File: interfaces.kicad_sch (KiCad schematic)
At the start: 125 parts, among them J3 USB-Micro-B-10118192-0001LF, J6 0878311420, J7 61300611121, U1 MTFC16GAPALNA-AIT, U14 XC7A100T-FGG484, U17 USB3300-EZK-TR, U18 USB3300-EZK-TR, U19 FT4232H_QFN, U21 LSF0108RKSR, U22 LSF0101DRYR, U23 ASEMB-24.000MHZ-LC-T, U24 ASEMB-24.000MHZ-LC-T, U6 NVT2008BQ,115, Y1 Oscillator_SMD_12MHz_KX-7

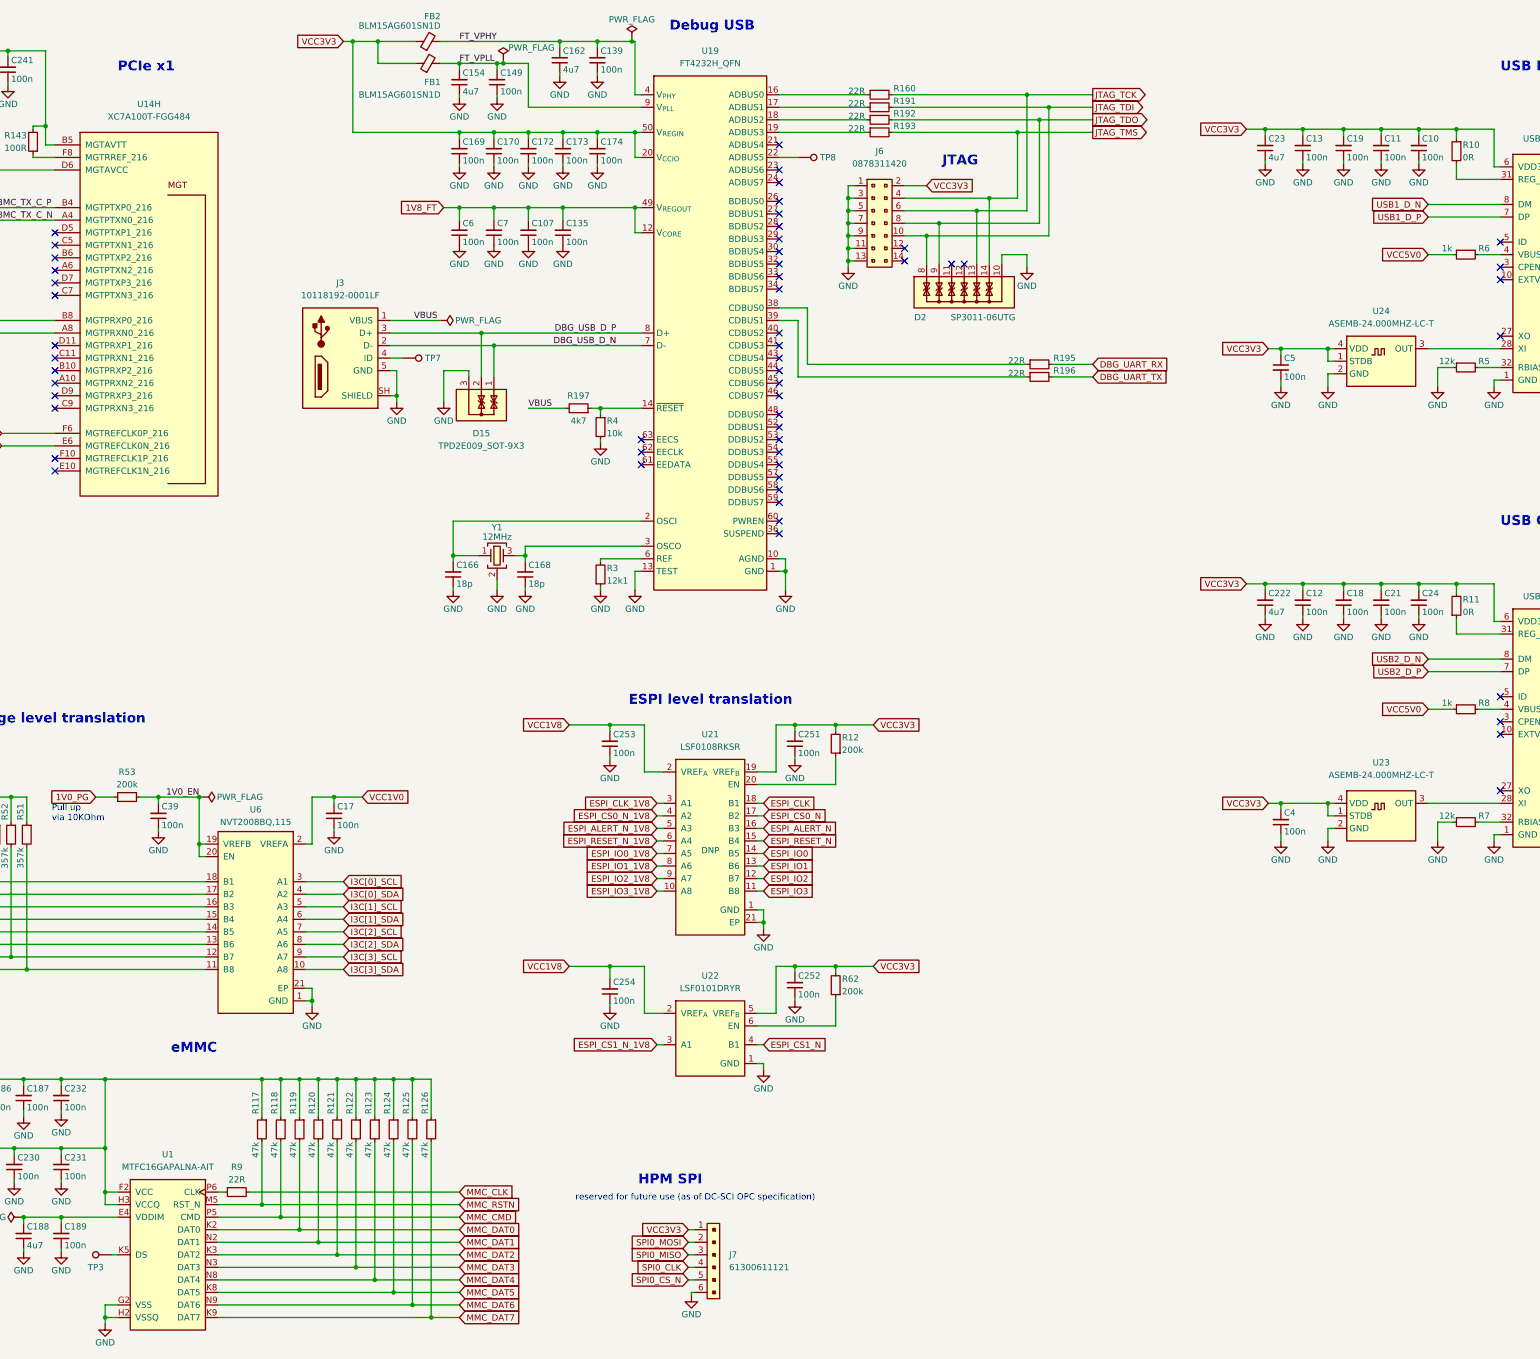
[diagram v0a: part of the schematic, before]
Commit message: [#55652] Fix hotareas
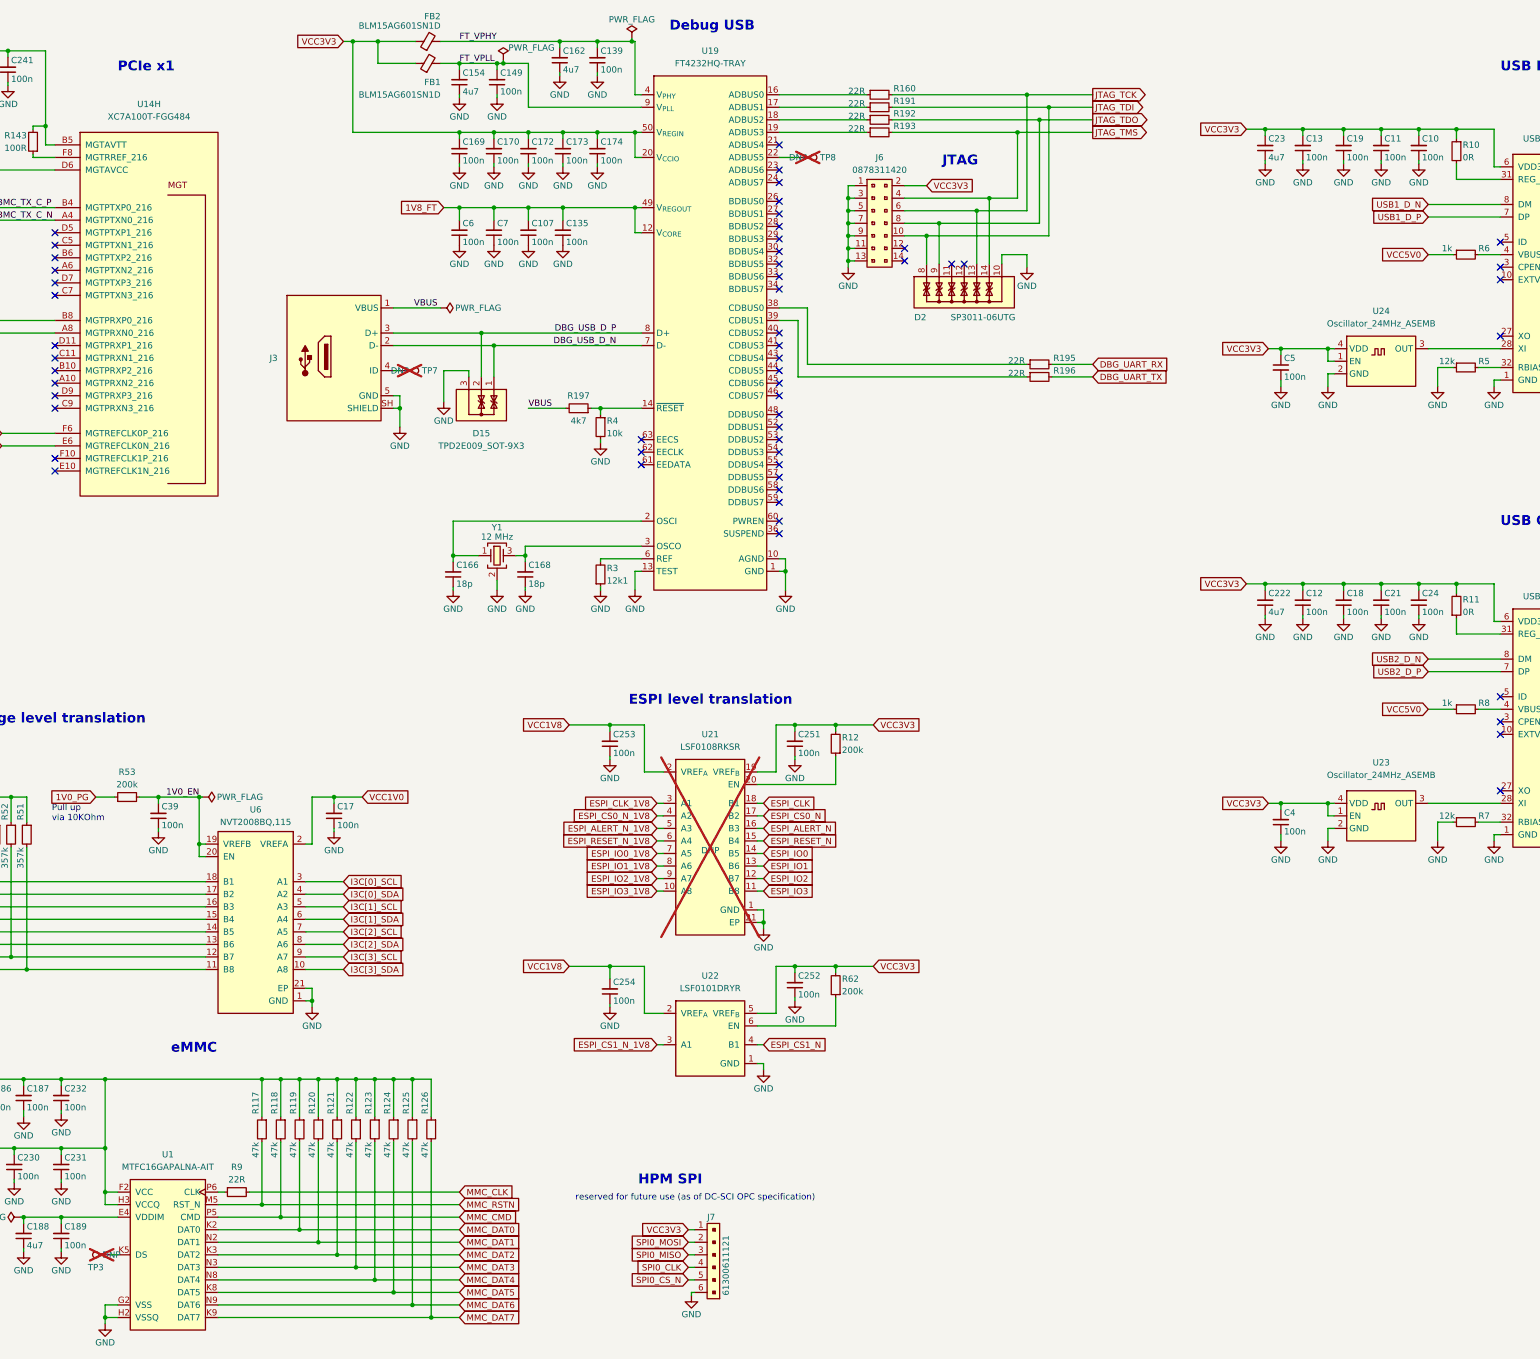
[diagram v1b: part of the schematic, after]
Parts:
- C166, C168: MPN MC0402N180J500CT -> CL05C180JB51PNC; Manufacturer Multicomp -> Samsung Electro-Mechanics
- D2: Manufacturer Littlefuse -> Littelfuse
- FB1, FB2: value FB_600Z_0.3A_0402 -> FB_600Z_0.3A_Murata-BLM15AG_0402; symbol antmicroFerriteBeadsandChips:FB_600Z_0.3A_0402 -> antmicroFerriteBeadsandChips:FB_600Z_0.3A_Murata-BLM15AG_0402
- J3: value USB-Micro-B-10118192-0001LF -> USB-Micro-B_Amphenol_10118192-0001LF; footprint antmicro-footprints:USB_Micro_B_Female_10118192 -> antmicro-footprints:USB-Micro-B_Receptacle_Amphenol_10118192; symbol antmicroUSBDVIHDMIConnectors:USB-Micro-B-10118192-0001LF -> antmicroUSBConnectors:USB-Micro-B_Amphenol_10118192-0001LF; VSD_class (none) -> USB Micro
- J6: value 0878311420 -> PinHeader_2x7_P2mm_Drill1mm_Shrouded; symbol antmicroRectangularConnectorsHeadersMalePins:PinHeader_2x7_P2mm_Drill1mm_Shrouded -> antmicroGenericPinHeaders:PinHeader_2x7_P2mm_Drill1mm_Shrouded
- J7: value 61300611121 -> PinHeader_1x6_P2.54mm_Drill1.1mm; footprint antmicro-footprints:PinHeader_1x6_P2.54mm -> antmicro-footprints:PinHeader_1x6_P2.54mm_Drill1.1mm; symbol antmicroRectangularConnectorsHeadersMalePins:61300611121 -> antmicroGenericPinHeaders:PinHeader_1x6_P2.54mm_Drill1.1mm
- R12, R53, R62: value R_200k_0402-artix-dc-scm -> R_200k_0402
- R45, R46, R47, R48, R49, R50, R51, R52: value R_357k_0402-artix-dc-scm -> R_357k_0402
- TP3, TP7, TP8: value TP_SMD1MM -> TP_1mm_SMD; footprint antmicro-footprints:Testpoint_smd_1mm -> antmicro-footprints:TP_SMD_1mm; now not fitted; now left out of the parts list
- U1: footprint antmicro-footprints:BGA-100_18x14mm_Layout17x10_P1mm -> antmicro-footprints:BGA-170-100_18x14mm_Layout17x10_P1mm; Manufacturer Micron -> Micron Technology
- U14: footprint antmicro-footprints:BGA-484_23x23mm_Layout22x22_P1mm_Xilinx_FGG484 -> antmicro-footprints:BGA-484_23x23mm_Layout22x22_P1mm_FGG484; symbol antmicroMicrocontrollers:XC7A100T-FGG484 -> antmicroFPGAChips:XC7A100T-FGG484; Manufacturer Xilinx -> AMD-Xilinx
- U17, U18: Manufacturer Microchip -> Microchip Technology
- U19: footprint antmicro-footprints:QFN-64_1EP_9x9mm_P0.5mm -> antmicro-footprints:QFN-64-1EP_9x9mm_P0.5mm; Manufacturer FTDI -> FTDI Chip
- U21: now not fitted; now left out of the parts list
- U23, U24: value ASEMB-24.000MHZ-LC-T -> Oscillator_24MHz_ASEMB; footprint antmicro-footprints:Oscillator_SMD_Abracon_ASEM_3.2x2.5mm -> antmicro-footprints:Oscillator_SMD_Abracon_ASEMB_3.2x2.5mm; symbol antmicroOscillators:Oscillator_SMD_24MHz_ASEMB -> antmicroOscillators:Oscillator_24MHz_ASEMB; Val 24MHz -> 24 MHz
- Y1: value Oscillator_SMD_12MHz_KX-7 -> Resonator_12MHz_ABM8G; footprint antmicro-footprints:Oscillator_SMD_Geyer_KX-7-4Pin_3.2x2.5mm -> antmicro-footprints:Resonator_SMD_Abracon_ABM8G_3.2x2.5mm; symbol antmicroCrystals:Oscillator_SMD_12MHz_KX-7 -> antmicroResonators:Resonator_12MHz_ABM8G; MPN ABM8G-12.000MHZ-18-D2Y-T -> ABM8G-12.000MHZ-18-D2Y-T; Val 12MHz -> 12 MHz

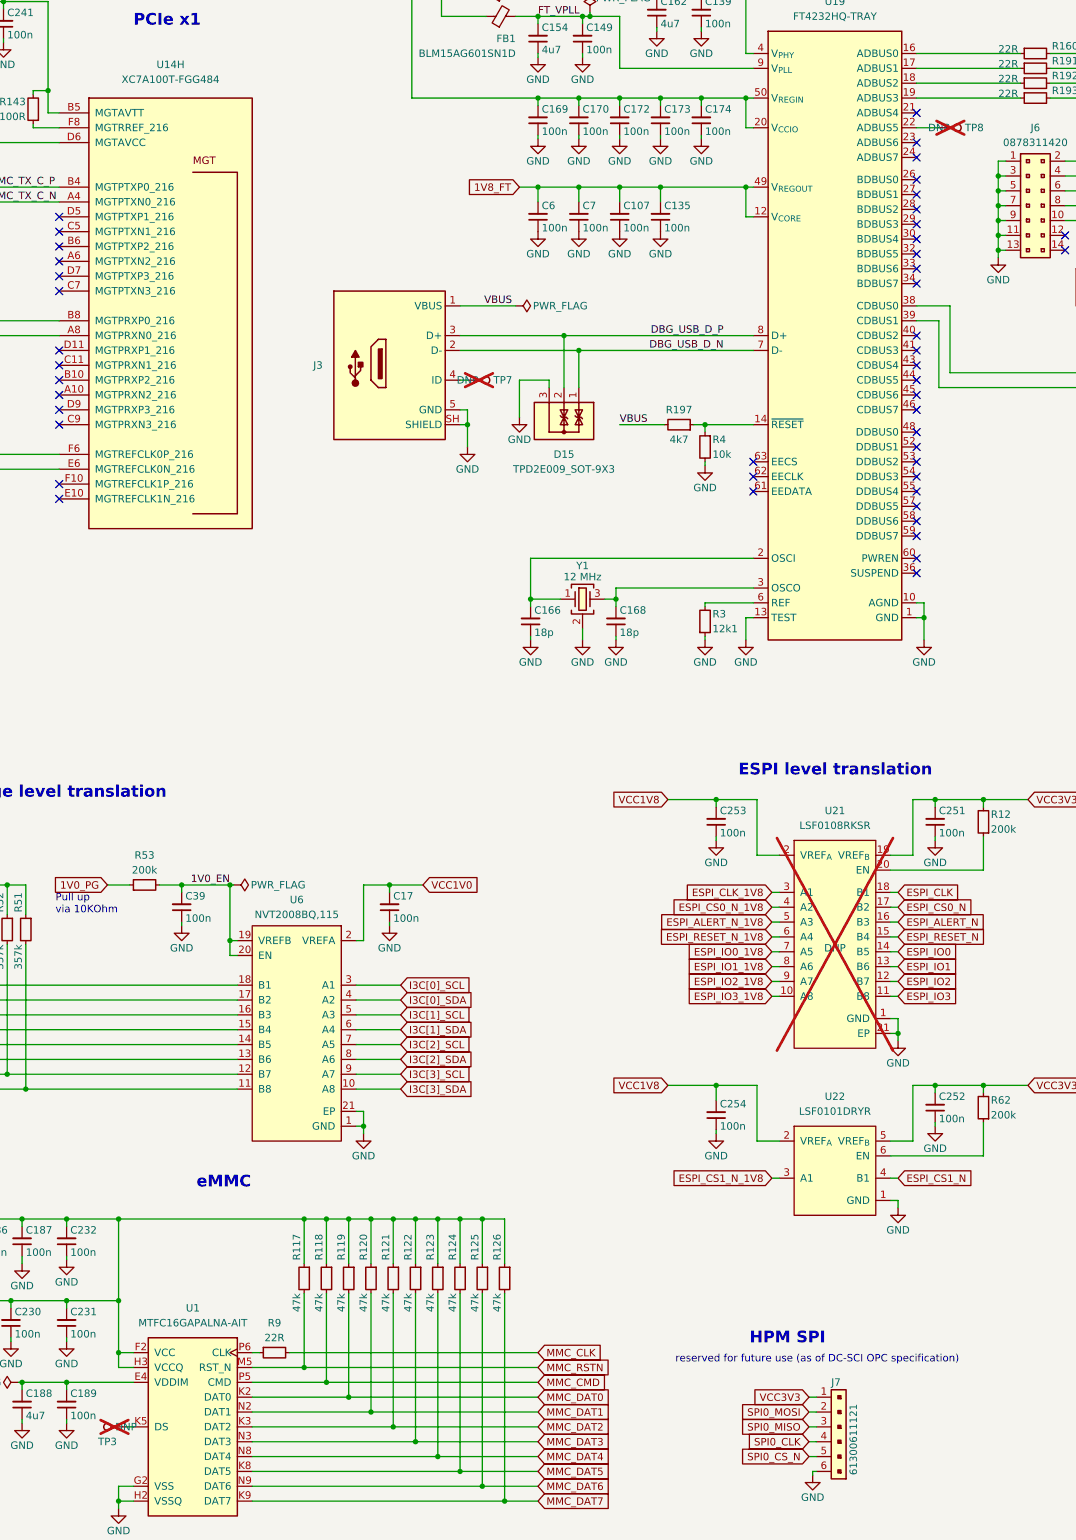
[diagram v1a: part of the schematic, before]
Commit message: [#68236] Update components description
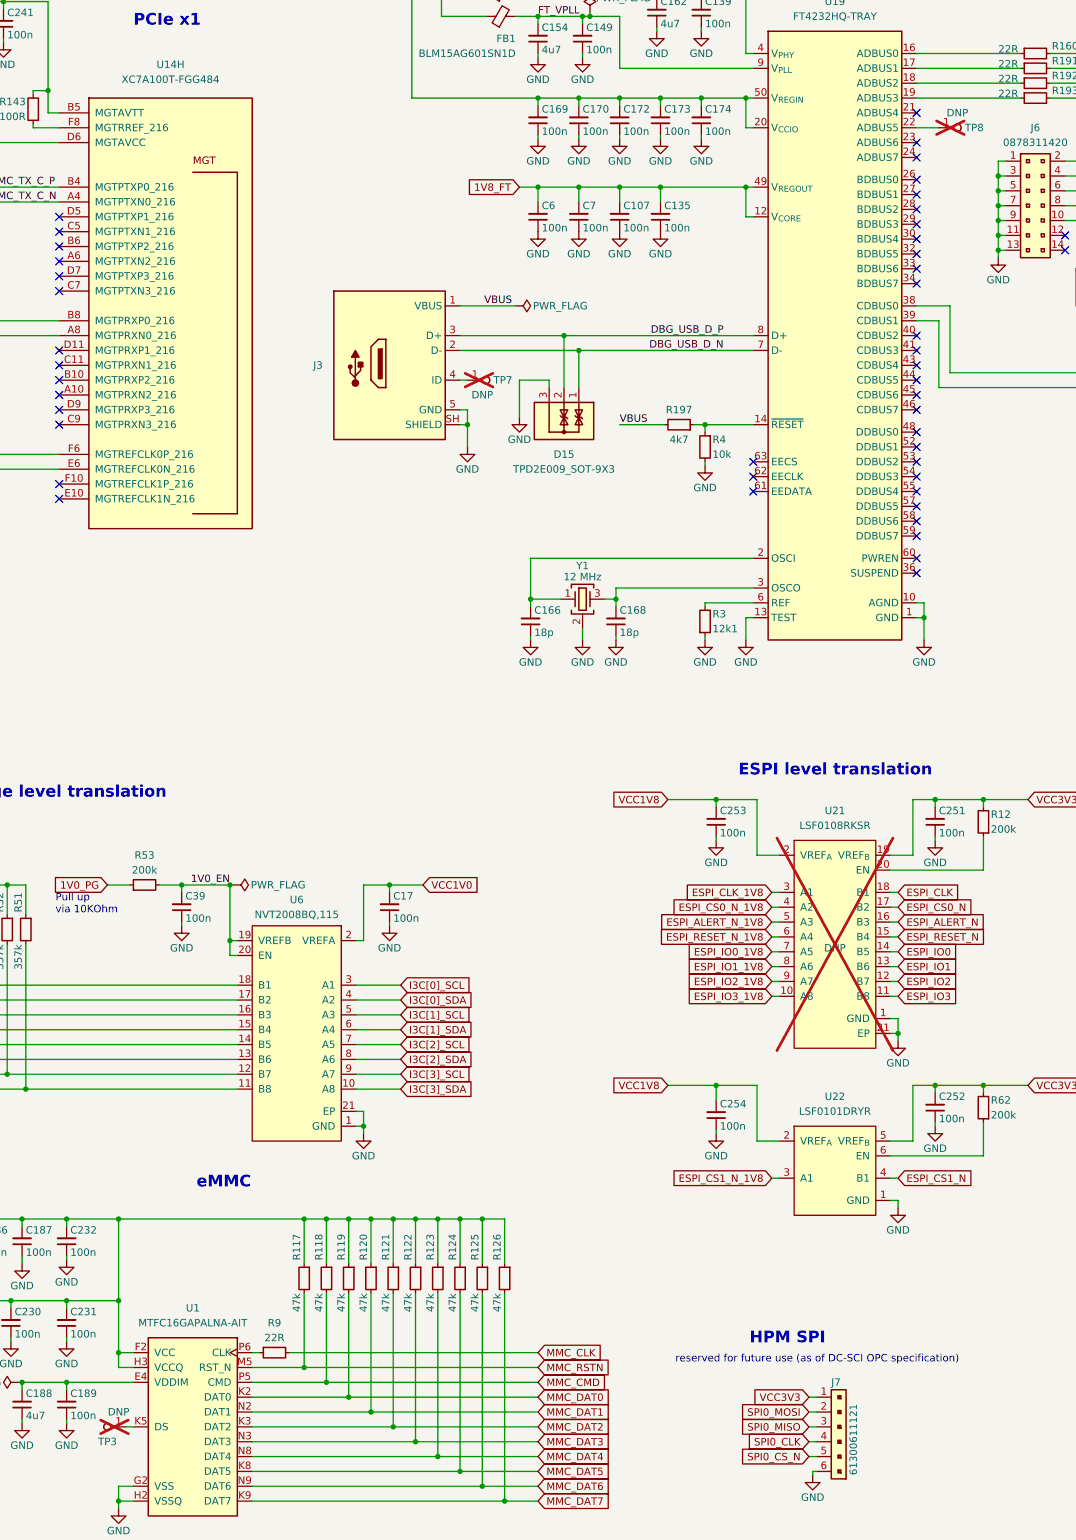
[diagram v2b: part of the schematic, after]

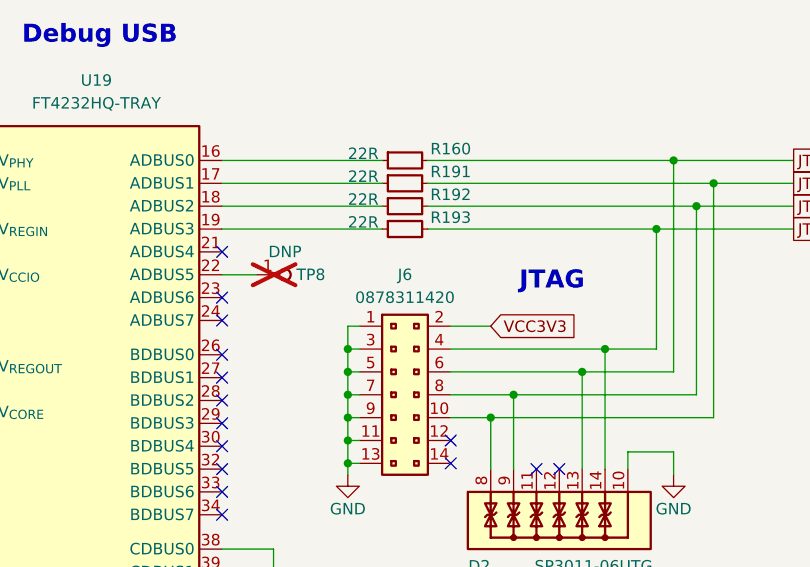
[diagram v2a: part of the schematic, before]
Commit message: [#68236] Update footprints for studs, J2 and U21
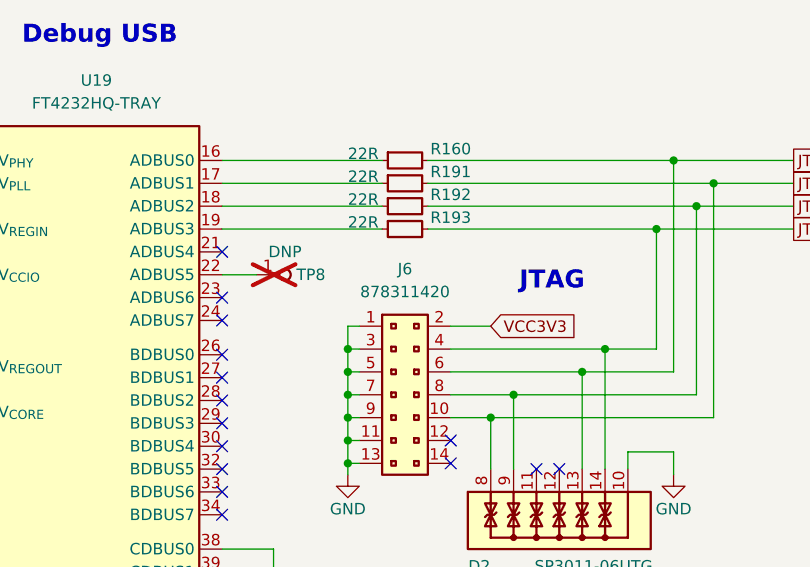
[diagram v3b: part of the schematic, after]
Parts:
- removed J6: PinHeader_2x7_P2mm_Drill1mm_Shrouded, antmicro-footprints:PinHeader_2x7_P2mm_Drill1mm_Shrouded, symbol antmicroGenericPinHeaders:PinHeader_2x7_P2mm_Drill1mm_Shrouded
- added J6: PinHeader_2x7_P2mm_Drill0.9mm_878311420, antmicro-footprints:PinHeader_2x7_P2mm_Drill0.9mm_878311420, symbol antmicroGenericPinHeaders:PinHeader_2x7_P2mm_Drill0.9mm_878311420
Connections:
- net GND: now also J6.1, J6.11, J6.13, J6.3, J6.5, J6.7, J6.9
- net JTAG_TCK: now also J6.6
- net JTAG_TDI: now also J6.10
- net JTAG_TDO: now also J6.8
- net JTAG_TMS: now also J6.4
- net VCC3V3: now also J6.2

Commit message: [#68236] Allign sch to grid
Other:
- moved on the sheet: C10, C107, C11, C13, C134, C139, C149, C154, C162, C166, C168, C169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
